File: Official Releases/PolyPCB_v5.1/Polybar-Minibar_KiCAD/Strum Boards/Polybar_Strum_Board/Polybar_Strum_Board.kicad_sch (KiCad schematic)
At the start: 21 parts, among them SW1 MX_SW_solder, SW2 MX_SW_solder, SW3 MX_SW_HS, SW4 MX_SW_HS, U1 ProMicro

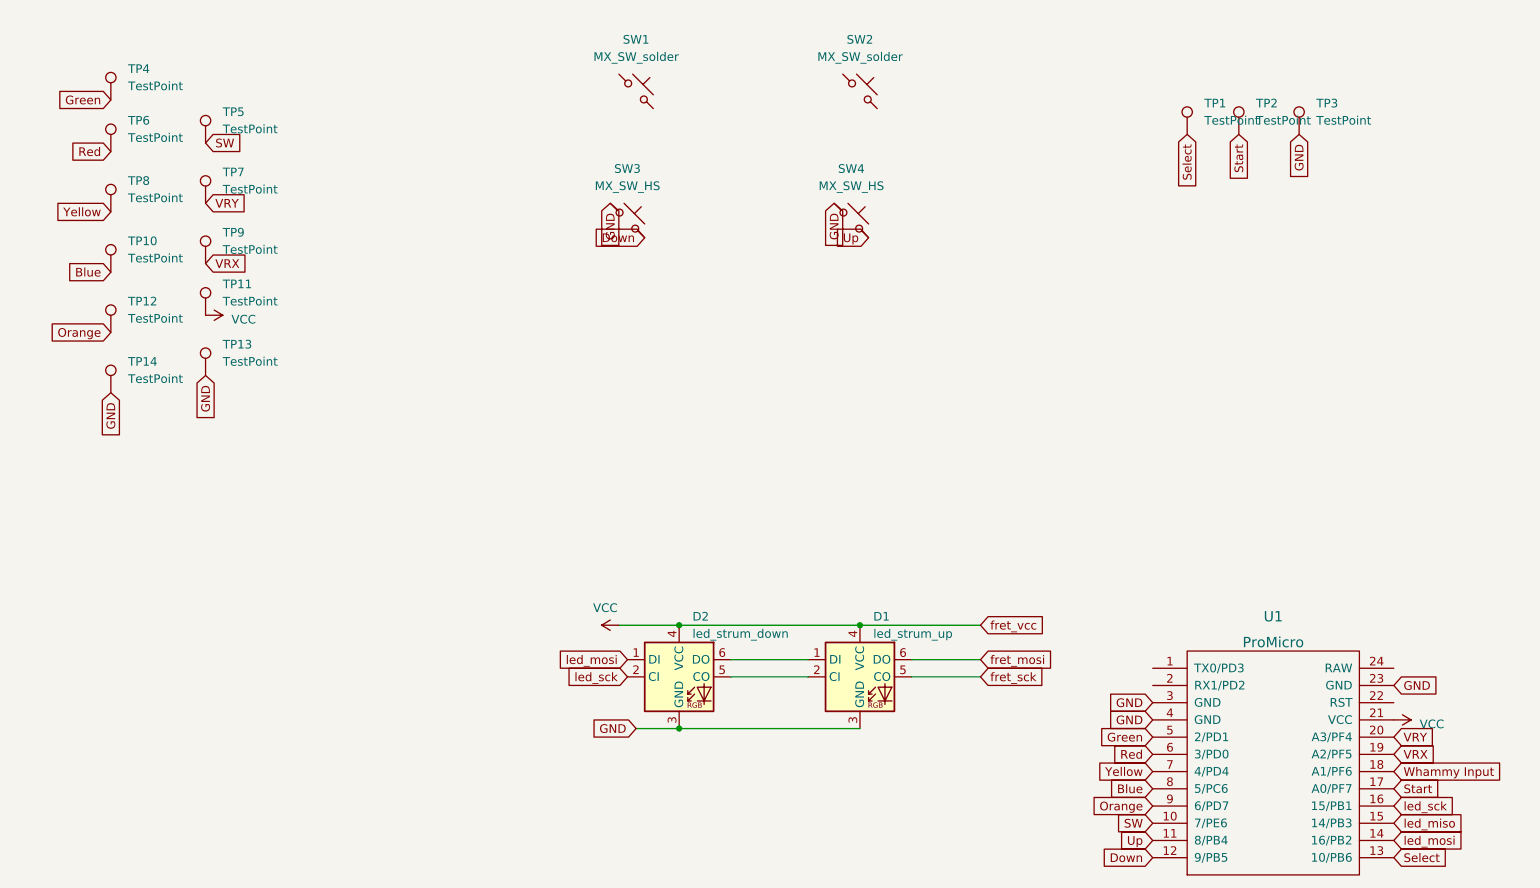
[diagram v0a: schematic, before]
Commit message: Linked everything in the PCB to the schematic
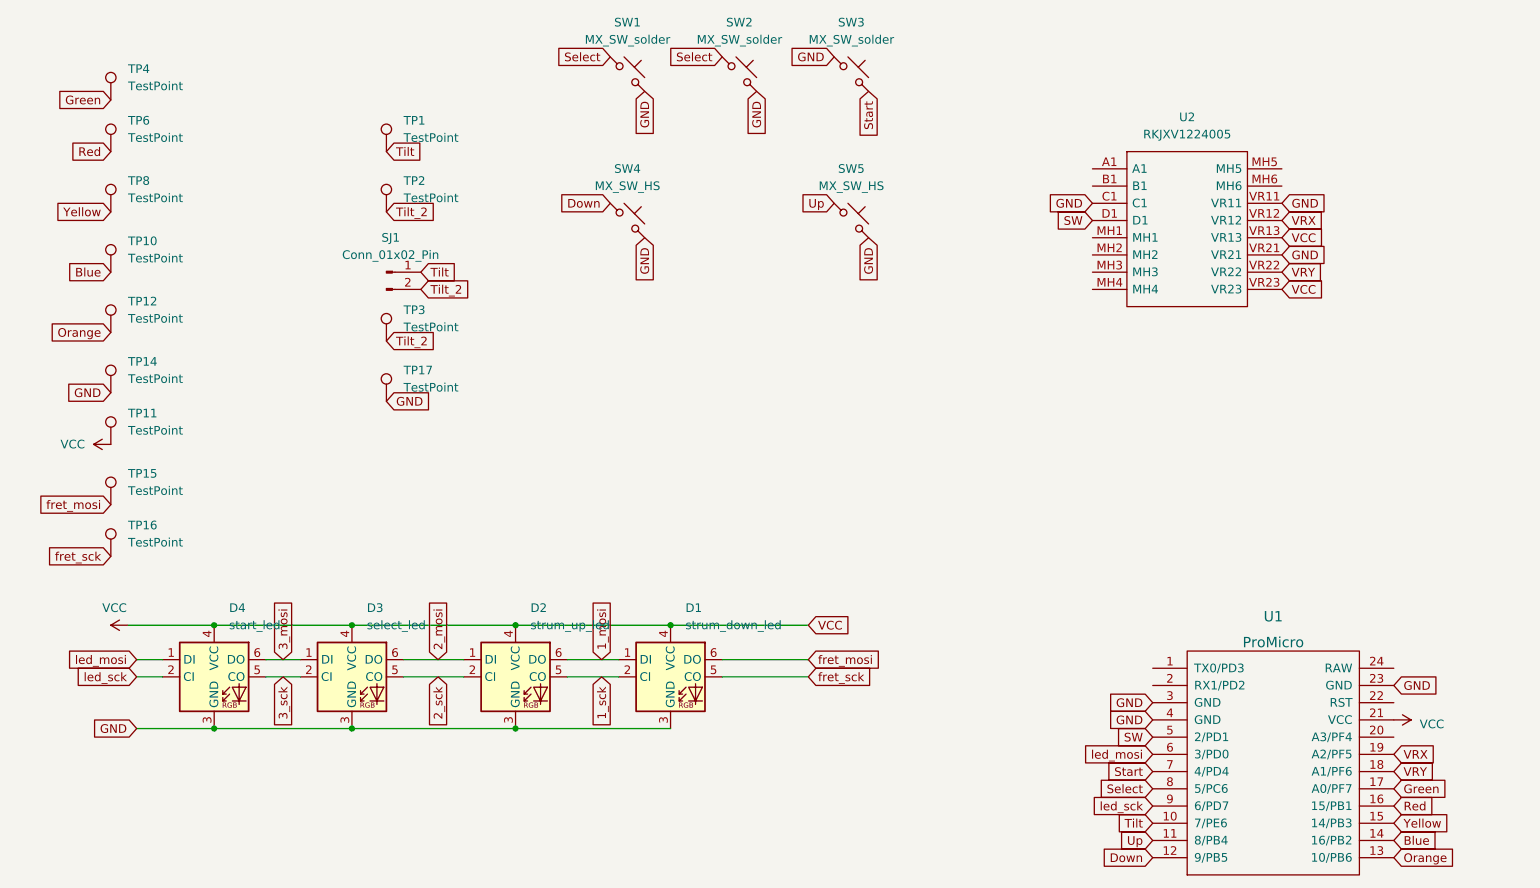
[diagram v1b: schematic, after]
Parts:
- removed TP13, TP5, TP7, TP9: TestPoint, TestPoint:TestPoint_THTPad_D3.0mm_Drill1.5mm, symbol Connector:TestPoint
- added D2: strum_up_led, LED_SMD:LED_RGB_5050-6, symbol LED:APA102
- added D3: select_led, LED_SMD:LED_RGB_5050-6, symbol LED:APA102
- added SJ1: Conn_01x02_Pin, Polybar:Solder_Jumper, symbol Connector:Conn_01x02_Pin
- added SW2: MX_SW_solder, Button_Switch_SMD:SW_SPST_PTS645, symbol marbastlib-mx:MX_SW_solder
- added TP15, TP16: TestPoint, Polybar:test_point, symbol Connector:TestPoint
- added TP17: TestPoint, Polybar:test_point_2, symbol Connector:TestPoint
- added U2: RKJXV1224005, RKJXV1224005, symbol Polybar:RKJXV1224005
- D1: value led_strum_up -> strum_down_led
- D4: renamed from D2; value led_strum_down -> start_led
- SW1: footprint marbastlib-mx:SW_MX_1u -> Button_Switch_SMD:SW_SPST_PTS645
- SW3: renamed from SW2; footprint marbastlib-mx:SW_MX_1u -> Button_Switch_SMD:SW_SPST_PTS645
- SW4: renamed from SW3; footprint marbastlib-mx:SW_MX_HS_1u -> Polybar:Kailh_Hotswap_MX
- SW5: renamed from SW4; footprint marbastlib-mx:SW_MX_HS_1u -> Polybar:Kailh_Hotswap_MX
- TP1, TP2, TP3: footprint TestPoint:TestPoint_THTPad_D3.0mm_Drill1.5mm -> Polybar:test_point_2
- TP10, TP11, TP12, TP14, TP4, TP6, TP8: footprint TestPoint:TestPoint_THTPad_D3.0mm_Drill1.5mm -> Polybar:test_point
- U1: footprint Keebio-Parts:ArduinoProMicro -> Polybar:KB2040-ProMicroPins
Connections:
- net Whammy Input is gone; now on net VRY: U1.18 (A1/PF6)
- net led_miso is gone; now on net Yellow: U1.15 (14/PB3)
- net Blue: now also U1.14 (16/PB2); no longer U1.8 (5/PC6)
- net Down: now also SW4.1; no longer SW4.2
- net GND: now also SW1.2, SW3.1, SW4.2, SW5.2, D2.3 (GND), D3.3 (GND), SW2.2, TP17.1, U2.C1, U2.VR11, U2.VR21; no longer SW4.1, SW5.1, TP3.1
- net Green: now also U1.17 (A0/PF7); no longer U1.5 (2/PD1)
- net Orange: now also U1.13 (10/PB6); no longer U1.9 (6/PD7)
- net Red: now also U1.16 (15/PB1); no longer U1.6 (3/PD0)
- net SW: now also U1.5 (2/PD1), U2.D1; no longer U1.10 (7/PE6)
- net Select: now also SW1.1, U1.8 (5/PC6), SW2.1; no longer TP1.1, U1.13 (10/PB6)
- net Start: now also SW3.2, U1.7 (4/PD4); no longer TP2.1, U1.17 (A0/PF7)
- net Up: now also SW5.1; no longer SW5.2
- net VCC: now also D2.4 (VCC), D3.4 (VCC), U2.VR13, U2.VR23
- net VRX: now also U2.VR12
- net VRY: now also U2.VR22; no longer U1.20 (A3/PF4)
- net Yellow: no longer U1.7 (4/PD4)
- net fret_mosi: now also TP15.1
- net fret_sck: now also TP16.1
- net led_mosi: now also U1.6 (3/PD0); no longer U1.14 (16/PB2)
- net led_sck: now also U1.9 (6/PD7); no longer U1.16 (15/PB1)
- net 1_mosi: now reaches D1.1 (DI)
- net 1_mosi: now also D2.6 (DO); no longer D4.6 (DO)
- net 1_sck: now reaches D1.2 (CI)
- net 1_sck: now also D2.5 (CO); no longer D4.5 (CO)
- new net 2_mosi: D2.1 (DI), D3.6 (DO)
- new net 2_sck: D2.2 (CI), D3.5 (CO)
- new net 3_mosi: D3.1 (DI), D4.6 (DO)
- new net 3_sck: D3.2 (CI), D4.5 (CO)
- new net Tilt: SJ1.1 (Pin_1), TP1.1, U1.10 (7/PE6)
- new net Tilt_2: SJ1.2 (Pin_2), TP2.1, TP3.1
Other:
- moved on the sheet: D4, SW1, SW3, TP11
